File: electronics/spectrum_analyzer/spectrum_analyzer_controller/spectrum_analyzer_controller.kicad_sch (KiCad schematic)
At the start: 45 parts, among them J1 AudioJack3, J2 Conn_02x03_Odd_Even, J3 Barrel_Jack_Switch, J4 Conn_01x10_Socket, J5 Conn_01x14_Socket, SW1 SW_SPDT, U1 MSGEQ7, U2 MSGEQ7, U3 ATtiny84-20P, U4 74HC595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

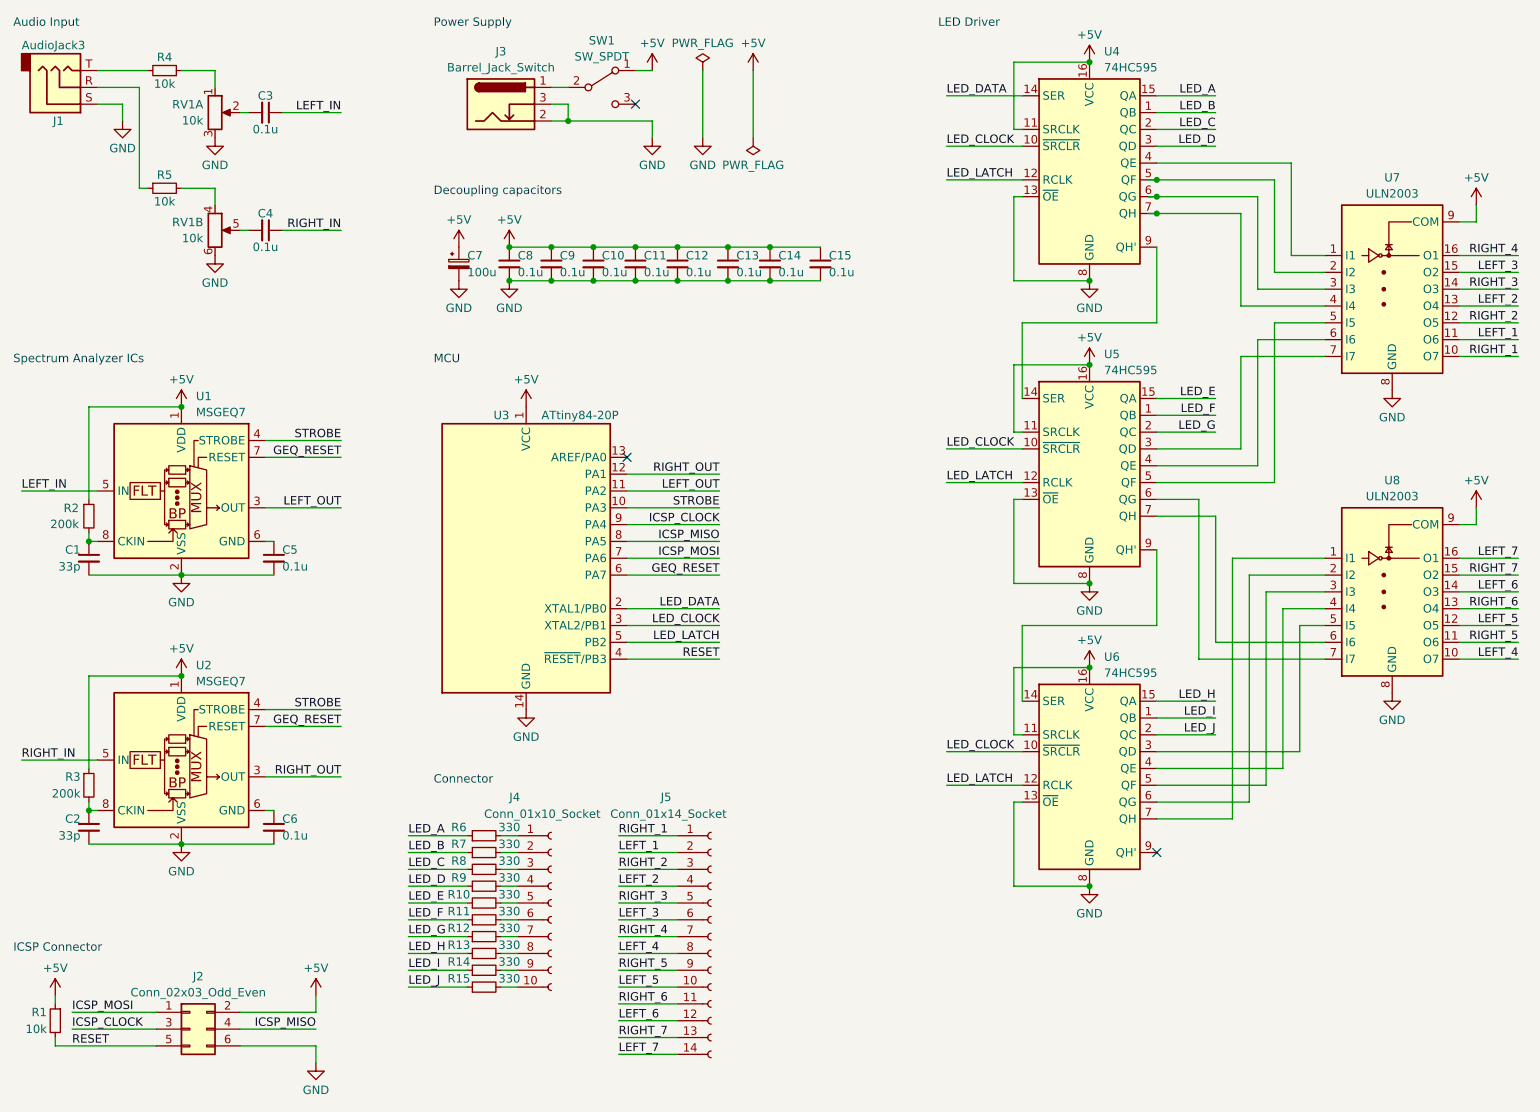
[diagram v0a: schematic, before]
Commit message: feat: change pcb layout and enclosure design
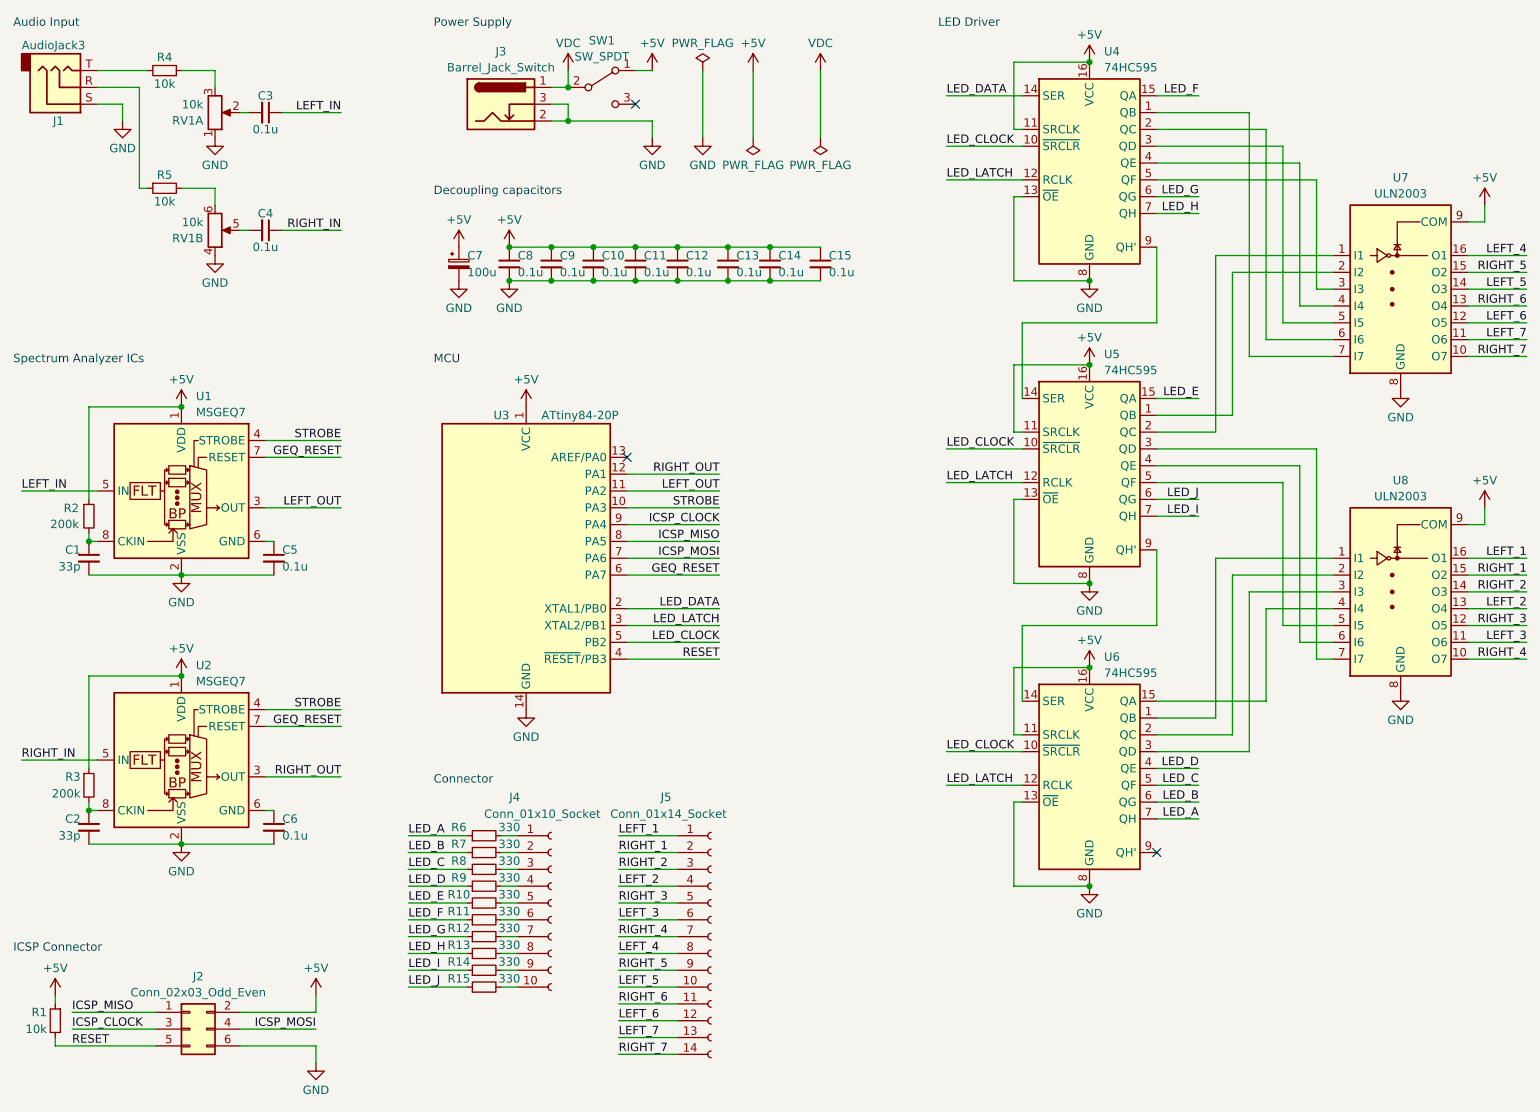
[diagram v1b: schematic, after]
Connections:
- net GND: now also RV1.1, RV1.4; no longer RV1.3, RV1.6
- net ICSP_MISO: now also J2.1 (Pin_1); no longer J2.4 (Pin_4)
- net ICSP_MOSI: now also J2.4 (Pin_4); no longer J2.1 (Pin_1)
- net LED_A: now also U6.7 (QH); no longer U4.15 (QA)
- net LED_B: now also U6.6 (QG); no longer U4.1 (QB)
- net LED_C: now also U6.5 (QF); no longer U4.2 (QC)
- net LED_CLOCK: now also U3.5 (PB2); no longer U3.3 (XTAL2/PB1)
- net LED_D: now also U6.4 (QE); no longer U4.3 (QD)
- net LED_F: now also U4.15 (QA); no longer U5.1 (QB)
- net LED_G: now also U4.6 (QG); no longer U5.2 (QC)
- net LED_H: now also U4.7 (QH); no longer U6.15 (QA)
- net LED_I: now also U5.7 (QH); no longer U6.1 (QB)
- net LED_J: now also U5.6 (QG); no longer U6.2 (QC)
- net LED_LATCH: now also U3.3 (XTAL2/PB1); no longer U3.5 (PB2)
- net LEFT_1: now also J5.1 (Pin_1), U8.16 (O1); no longer J5.2 (Pin_2), U7.11 (O6)
- net LEFT_2: now also U8.13 (O4); no longer U7.13 (O4)
- net LEFT_3: now also U8.11 (O6); no longer U7.15 (O2)
- net LEFT_4: now also U7.16 (O1); no longer U8.10 (O7)
- net LEFT_5: now also U7.14 (O3); no longer U8.12 (O5)
- net LEFT_6: now also U7.12 (O5); no longer U8.14 (O3)
- net LEFT_7: now also J5.13 (Pin_13), U7.11 (O6); no longer J5.14 (Pin_14), U8.16 (O1)
- net RIGHT_1: now also J5.2 (Pin_2), U8.15 (O2); no longer J5.1 (Pin_1), U7.10 (O7)
- net RIGHT_2: now also U8.14 (O3); no longer U7.12 (O5)
- net RIGHT_3: now also U8.12 (O5); no longer U7.14 (O3)
- net RIGHT_4: now also U8.10 (O7); no longer U7.16 (O1)
- net RIGHT_5: now also U7.15 (O2); no longer U8.11 (O6)
- net RIGHT_6: now also U7.13 (O4); no longer U8.13 (O4)
- net RIGHT_7: now also J5.14 (Pin_14), U7.10 (O7); no longer J5.13 (Pin_13), U8.15 (O2)
- net at U6.3 (QD): now also U8.3 (I3); no longer U8.5 (I5)
- net at U8.4 (I4): now also U6.15 (QA); no longer U6.4 (QE)
- net at U8.2 (I2): now also U6.2 (QC); no longer U6.6 (QG)
- net at U8.1 (I1): now also U6.1 (QB); no longer U6.7 (QH)
- net at R5.2: now also RV1.6; no longer RV1.4
- net VDC: now reaches J3.1, SW1.2 (B)
- net at U7.1 (I1): now also U5.2 (QC); no longer U4.4 (QE)
- net at U7.2 (I2): now also U5.1 (QB); no longer U4.5 (QF)
- net at U7.3 (I3): now also U4.5 (QF); no longer U4.6 (QG)
- net at U7.4 (I4): now also U4.4 (QE); no longer U4.7 (QH)
- net at U7.5 (I5): now also U4.3 (QD); no longer U5.5 (QF)
- net at U7.6 (I6): now also U4.2 (QC); no longer U5.4 (QE)
- net at U7.7 (I7): now also U4.1 (QB); no longer U5.3 (QD)
- net at R4.1: now also RV1.3; no longer RV1.1
- net at U8.7 (I7): now also U5.3 (QD); no longer U5.6 (QG)
- net at U8.6 (I6): now also U5.4 (QE); no longer U5.7 (QH)
- new net: U5.5 (QF), U8.5 (I5)
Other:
- moved on the sheet: U7, U8
